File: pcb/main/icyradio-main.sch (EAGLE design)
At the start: 702 parts, among them CON101 FPC-22P, CON102 FPC-22P, CON1101 2EDG-2P-5MM-H, CON701 4P-SH-TOP, CON801 PCIE-X4-EDGE, J101 RJ45_MAG_LED_1G-TE-1-2301994-0, J701 TRSJACK, J702 TRSJACK, J703 TRSJACK, M701 SPH0641LM4H-1, M702 SPH0641LM4H-1, Q101 AO3400, Q102 AO3400, Q1101 AO3400, Q1102 AO4805, Q1103 AO3400, Q1104 AO4805, Q1105 AO4805, Q1106 AO3400, T501 UWB1-85E, T502 UWB1-85E, T503 UWB1-85E, T504 UWB1-85E, T505 UWB1-85E, T506 UWB1-85E, T507 UWB1-85E, T508 UWB1-85E, U1001 LTC4313-3, U1002 UPD301C, U1003 MIC2019, U101 MIC2019, U102 RPI-CM4, U1101 MCP1804-3302, U1102 LT7182S, U1201 ADM7172ACPZ-5.0, U1202 ADM7171ACPZ-1.3, U1203 ADM7171ACPZ-3.3, U1204 MIC23159, U1205 MIC5166, U1206 ADM7171ACPZ-1.3, U1207 ADM7171ACPZ-3.3, U1208 MIC23159, U1209 MIC23155, U1210 ADP7142AUJZ-3.3, U201 XC7A100TFGG484, U202 SST26VF064B, U301 MT41K256M16TW-125, U401 AD9361, U501 MIC2019, U502 MIC2019, U503 MIC2019, U504 MIC2019, U505 ADL5601, U506 ADL5601, U601 8V97003, U701 ADAU1372, U901 DSB321SDA, U902 SI5351C-B-GM

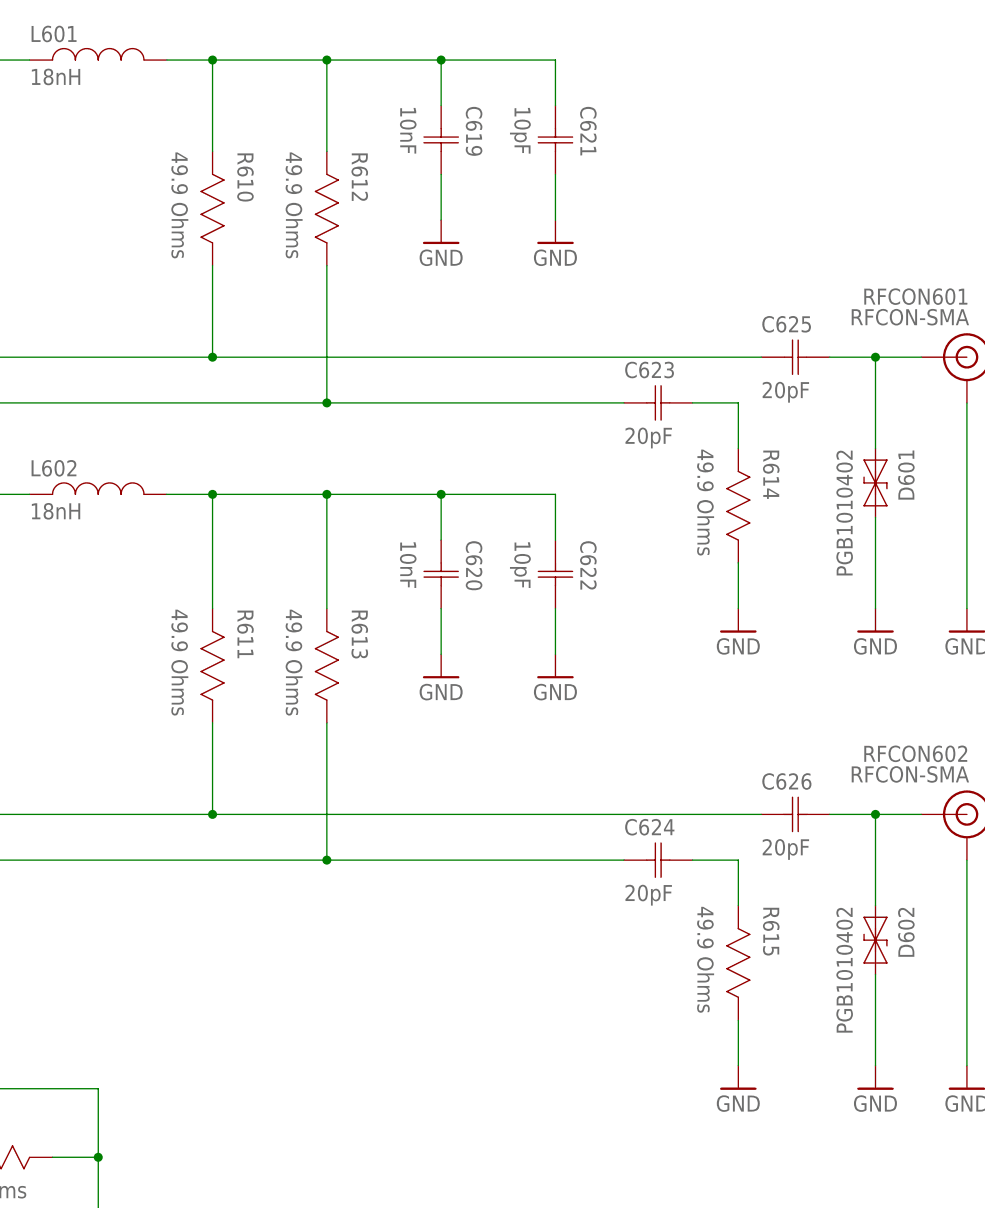
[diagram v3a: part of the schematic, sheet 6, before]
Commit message: Add new 8V97003 datasheet Add cooling fan expansion card (WIP) Updated some schematic resistors from 49.9R to 50R Sync mmWave expansion card firmware after some lab testing (WIP) Sync PMC firmware Sync RV firmware (WIP) Sync misc SoapySDR library work
Signed-off-by: João Silva <jgc3silva@gmail.com>
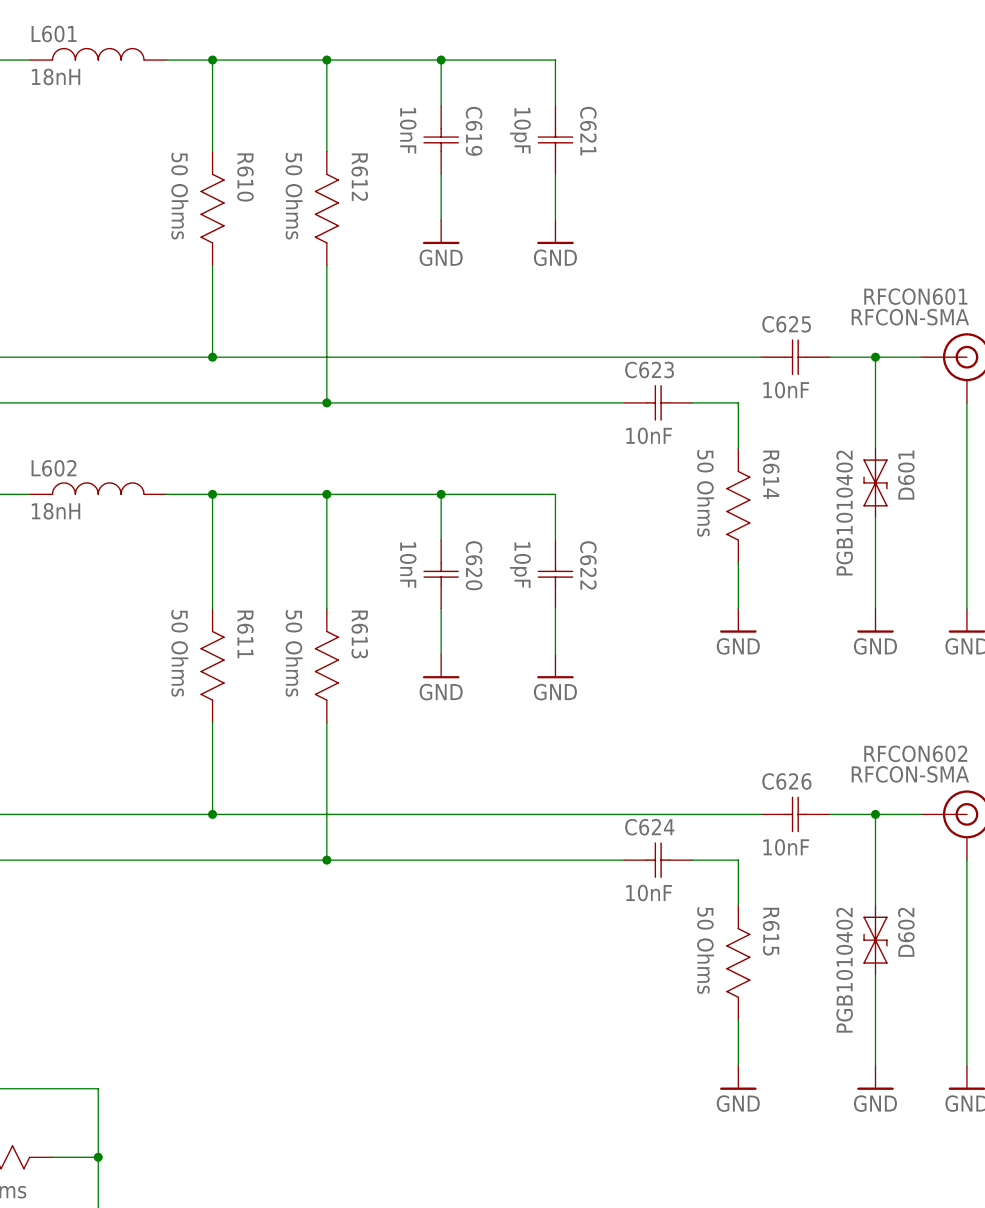
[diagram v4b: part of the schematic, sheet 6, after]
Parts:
- C619, C620: SERIES (none) -> ATC520L
- C623, C624, C625, C626: value 20pF -> 10nF; SERIES (none) -> ATC520L
- R610, R611, R612, R613, R614, R615: value 49.9 Ohms -> 50 Ohms; SERIES (none) -> FC0402
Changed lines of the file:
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@@
 <part name="C606" library="Capacitor" deviceset="CAPACITOR" device="-0402" value="22uF"/>
 <part name="GND278" library="Supply Symbol" deviceset="GND" device=""/>
-<part name="R611" library="Resistor" deviceset="RESISTOR" device="-0402" value="49.9 Ohms"/>
-<part name="R613" library="Resistor" deviceset="RESISTOR" device="-0402" value="49.9 Ohms"/>
+<part name="R611" library="Resistor" deviceset="RESISTOR" device="-0402" value="50 Ohms">
+<attribute name="SERIES" value="FC0402"/>
+</part>
+<part name="R613" library="Resistor" deviceset="RESISTOR" device="-0402" value="50 Ohms">
+<attribute name="SERIES" value="FC0402"/>
+</part>
 <part name="C601" library="Capacitor" deviceset="CAPACITOR" device="-0402" value="100nF"/>
 <part name="R604" library="Resistor" deviceset="RESISTOR" device="-0402" value="1K Ohms"/>
@@
 <part name="C615" library="Capacitor" deviceset="CAPACITOR" device="-0402" value="1uF"/>
 <part name="GND427" library="Supply Symbol" deviceset="GND" device=""/>
-<part name="C626" library="Capacitor" deviceset="CAPACITOR" device="-0402" value="20pF"/>
-<part name="C624" library="Capacitor" deviceset="CAPACITOR" device="-0402" value="20pF"/>
-<part name="R615" library="Resistor" deviceset="RESISTOR" device="-0402" value="49.9 Ohms"/>
+<part name="C626" library="Capacitor" deviceset="CAPACITOR" device="-0402" value="10nF">
+<attribute name="SERIES" value="ATC520L"/>
+</part>
+<part name="C624" library="Capacitor" deviceset="CAPACITOR" device="-0402" value="10nF">
+<attribute name="SERIES" value="ATC520L"/>
+</part>
+<part name="R615" library="Resistor" deviceset="RESISTOR" device="-0402" value="50 Ohms">
+<attribute name="SERIES" value="FC0402"/>
+</part>
 <part name="GND428" library="Supply Symbol" deviceset="GND" device=""/>
-<part name="C625" library="Capacitor" deviceset="CAPACITOR" device="-0402" value="20pF"/>
-<part name="R614" library="Resistor" deviceset="RESISTOR" device="-0402" value="49.9 Ohms"/>
+<part name="C625" library="Capacitor" deviceset="CAPACITOR" device="-0402" value="10nF">
+<attribute name="SERIES" value="ATC520L"/>
+</part>
+<part name="R614" library="Resistor" deviceset="RESISTOR" device="-0402" value="50 Ohms">
+<attribute name="SERIES" value="FC0402"/>
+</part>
 <part name="GND429" library="Supply Symbol" deviceset="GND" device=""/>
-<part name="C623" library="Capacitor" deviceset="CAPACITOR" device="-0402" value="20pF"/>
-<part name="R610" library="Resistor" deviceset="RESISTOR" device="-0402" value="49.9 Ohms"/>
-<part name="R612" library="Resistor" deviceset="RESISTOR" device="-0402" value="49.9 Ohms"/>
+<part name="C623" library="Capacitor" deviceset="CAPACITOR" device="-0402" value="10nF">
+<attribute name="SERIES" value="ATC520L"/>
+</part>
+<part name="R610" library="Resistor" deviceset="RESISTOR" device="-0402" value="50 Ohms">
+<attribute name="SERIES" value="FC0402"/>
+</part>
+<part name="R612" library="Resistor" deviceset="RESISTOR" device="-0402" value="50 Ohms">
+<attribute name="SERIES" value="FC0402"/>
+</part>
 <part name="L601" library="Inductor" deviceset="INDUCTOR" device="-0402" value="18nH"/>
-<part name="C619" library="Capacitor" deviceset="CAPACITOR" device="-0402" value="10nF"/>
+<part name="C619" library="Capacitor" deviceset="CAPACITOR" device="-0402" value="10nF">
+<attribute name="SERIES" value="ATC520L"/>
+</part>
 <part name="GND430" library="Supply Symbol" deviceset="GND" device=""/>
 <part name="L602" library="Inductor" deviceset="INDUCTOR" device="-0402" value="18nH"/>
-<part name="C620" library="Capacitor" deviceset="CAPACITOR" device="-0402" value="10nF"/>
+<part name="C620" library="Capacitor" deviceset="CAPACITOR" device="-0402" value="10nF">
+<attribute name="SERIES" value="ATC520L"/>
+</part>
 <part name="GND431" library="Supply Symbol" deviceset="GND" device=""/>
 <part name="R608" library="Resistor" deviceset="RESISTOR" device="-0402" value="20 Ohms"/>
@@
 <attribute name="TOLERANCE" x="368.0714" y="205.74" size="1.778" layer="97" ratio="10" rot="SR270" align="top-left"/>
 <attribute name="POWER" x="365.5314" y="205.74" size="1.778" layer="97" ratio="10" rot="SR270" align="top-left"/>
+<attribute name="SERIES" x="373.38" y="205.74" size="1.778" layer="96" rot="R270" display="off"/>
 </instance>
 <instance part="R613" gate="G$1" x="386.08" y="205.74" smashed="yes" rot="R270">
@@
 <attribute name="TOLERANCE" x="380.7714" y="205.74" size="1.778" layer="97" ratio="10" rot="SR270" align="top-left"/>
 <attribute name="POWER" x="378.2314" y="205.74" size="1.778" layer="97" ratio="10" rot="SR270" align="top-left"/>
+<attribute name="SERIES" x="386.08" y="205.74" size="1.778" layer="96" rot="R270" display="off"/>
 </instance>
 <instance part="C601" gate="G$1" x="137.16" y="139.7" smashed="yes">
@@
 <attribute name="NAME" x="434.34" y="185.6486" size="1.778" layer="95" ratio="10" rot="SR0"/>
 <attribute name="VOLTAGE" x="434.34" y="177.5714" size="1.778" layer="97" ratio="10" rot="SR0" align="top-left"/>
+<attribute name="SERIES" x="434.34" y="182.88" size="1.778" layer="96" display="off"/>
 </instance>
 <instance part="C624" gate="G$1" x="419.1" y="177.8" smashed="yes">
@@
 <attribute name="NAME" x="419.1" y="180.5686" size="1.778" layer="95" ratio="10" rot="SR0"/>
 <attribute name="VOLTAGE" x="419.1" y="172.4914" size="1.778" layer="97" ratio="10" rot="SR0" align="top-left"/>
+<attribute name="SERIES" x="419.1" y="177.8" size="1.778" layer="96" display="off"/>
 </instance>
 <instance part="R615" gate="G$1" x="431.8" y="172.72" smashed="yes" rot="R270">
@@
 <attribute name="TOLERANCE" x="426.4914" y="172.72" size="1.778" layer="97" ratio="10" rot="SR270" align="top-left"/>
 <attribute name="POWER" x="423.9514" y="172.72" size="1.778" layer="97" ratio="10" rot="SR270" align="top-left"/>
+<attribute name="SERIES" x="431.8" y="172.72" size="1.778" layer="96" rot="R270" display="off"/>
 </instance>
 <instance part="GND428" gate="G$1" x="431.8" y="154.94" smashed="yes">
@@
 <attribute name="NAME" x="434.34" y="236.4486" size="1.778" layer="95" ratio="10" rot="SR0"/>
 <attribute name="VOLTAGE" x="434.34" y="228.3714" size="1.778" layer="97" ratio="10" rot="SR0" align="top-left"/>
+<attribute name="SERIES" x="434.34" y="233.68" size="1.778" layer="96" display="off"/>
 </instance>
 <instance part="R614" gate="G$1" x="431.8" y="223.52" smashed="yes" rot="R270">
@@
 <attribute name="TOLERANCE" x="426.4914" y="223.52" size="1.778" layer="97" ratio="10" rot="SR270" align="top-left"/>
 <attribute name="POWER" x="423.9514" y="223.52" size="1.778" layer="97" ratio="10" rot="SR270" align="top-left"/>
+<attribute name="SERIES" x="431.8" y="223.52" size="1.778" layer="96" rot="R270" display="off"/>
 </instance>
 <instance part="GND429" gate="G$1" x="431.8" y="205.74" smashed="yes">
@@
 <attribute name="NAME" x="419.1" y="231.3686" size="1.778" layer="95" ratio="10" rot="SR0"/>
 <attribute name="VOLTAGE" x="419.1" y="223.2914" size="1.778" layer="97" ratio="10" rot="SR0" align="top-left"/>
+<attribute name="SERIES" x="419.1" y="228.6" size="1.778" layer="96" display="off"/>
 </instance>
 <instance part="R610" gate="G$1" x="373.38" y="256.54" smashed="yes" rot="R270">
@@
 <attribute name="TOLERANCE" x="368.0714" y="256.54" size="1.778" layer="97" ratio="10" rot="SR270" align="top-left"/>
 <attribute name="POWER" x="365.5314" y="256.54" size="1.778" layer="97" ratio="10" rot="SR270" align="top-left"/>
+<attribute name="SERIES" x="373.38" y="256.54" size="1.778" layer="96" rot="R270" display="off"/>
 </instance>
 <instance part="R612" gate="G$1" x="386.08" y="256.54" smashed="yes" rot="R270">
@@
 <attribute name="TOLERANCE" x="380.7714" y="256.54" size="1.778" layer="97" ratio="10" rot="SR270" align="top-left"/>
 <attribute name="POWER" x="378.2314" y="256.54" size="1.778" layer="97" ratio="10" rot="SR270" align="top-left"/>
+<attribute name="SERIES" x="386.08" y="256.54" size="1.778" layer="96" rot="R270" display="off"/>
 </instance>
 <instance part="L601" gate="G$1" x="353.06" y="266.7" smashed="yes">
@@
 <attribute name="NAME" x="401.5486" y="261.62" size="1.778" layer="95" ratio="10" rot="SR270"/>
 <attribute name="VOLTAGE" x="393.4714" y="261.62" size="1.778" layer="97" ratio="10" rot="SR270" align="top-left"/>
+<attribute name="SERIES" x="398.78" y="261.62" size="1.778" layer="96" rot="R270" display="off"/>
 </instance>
 <instance part="GND430" gate="G$1" x="398.78" y="248.92" smashed="yes">
@@
 <attribute name="NAME" x="401.5486" y="213.36" size="1.778" layer="95" ratio="10" rot="SR270"/>
 <attribute name="VOLTAGE" x="393.4714" y="213.36" size="1.778" layer="97" ratio="10" rot="SR270" align="top-left"/>
+<attribute name="SERIES" x="398.78" y="213.36" size="1.778" layer="96" rot="R270" display="off"/>
 </instance>
 <instance part="GND431" gate="G$1" x="398.78" y="200.66" smashed="yes">
